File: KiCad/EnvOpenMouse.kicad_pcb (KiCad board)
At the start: 2 copper layers, 34 x 106.6 mm, 117 parts, among them J1 Button, J10 0.8mm BM03B, J11 Conn_02x02_Top_Bottom, J12 0.8mm BM03B, J13 0.8mm BM03B, J2 Conn_01x03, J3 Button, J4 Conn_02x02_Top_Bottom, J5 Conn_02x02_Top_Bottom, J6 Conn_02x02_Top_Bottom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

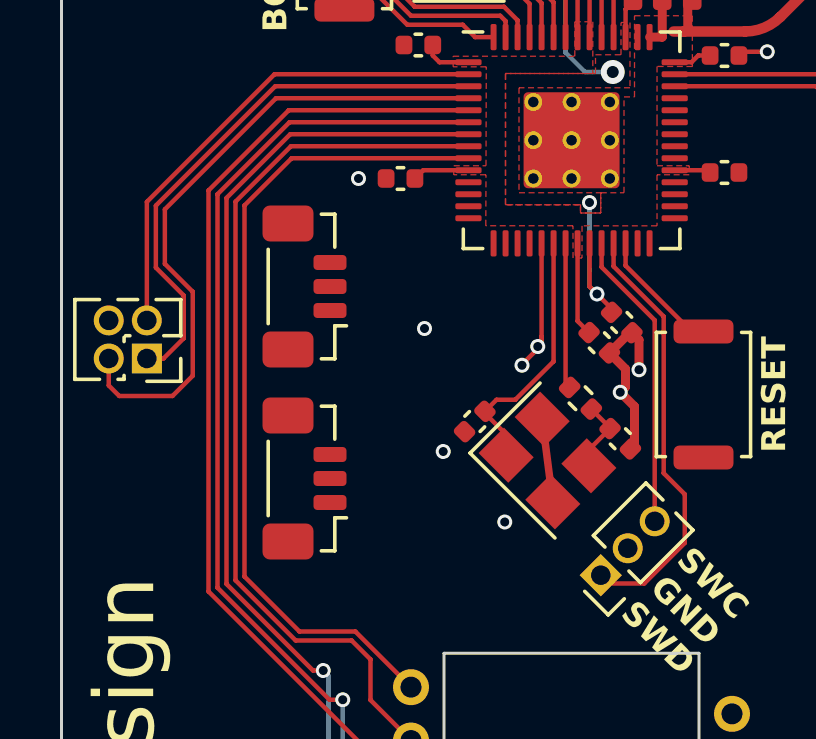
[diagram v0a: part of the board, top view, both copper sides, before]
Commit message: Added missing connections.
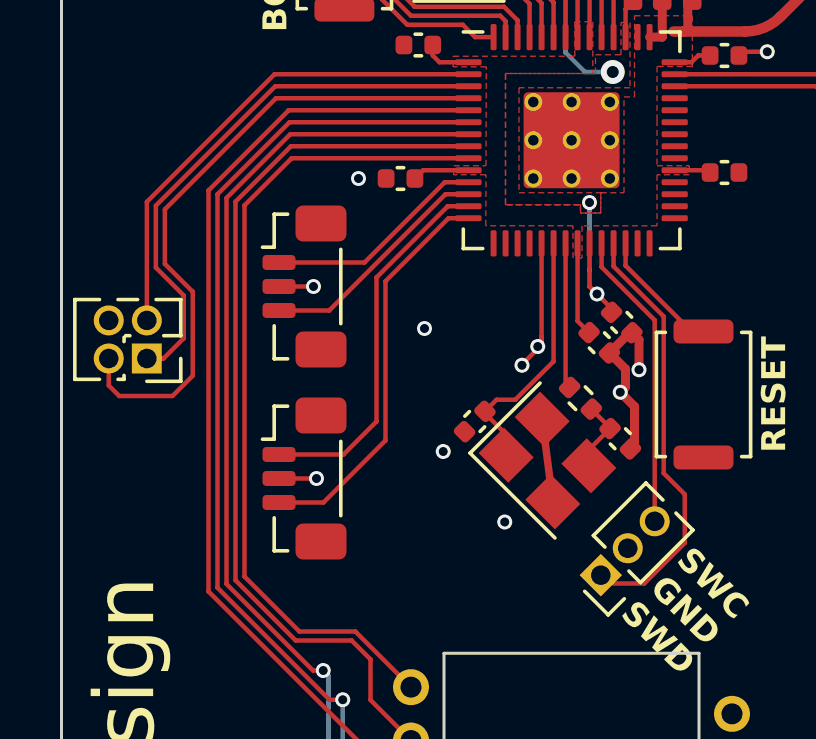
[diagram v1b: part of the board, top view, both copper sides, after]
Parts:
- turned J12 to -90 degrees
- turned J13 to -90 degrees
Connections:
- U3 pad 11: /RP2040/GPIO8 -> SB-1-A_MB
- U3 pad 12: /RP2040/GPIO9 -> SB-2-A_MB
- U3 pad 13: /RP2040/GPIO10 -> SB-3-A_MB
- U3 pad 14: /RP2040/GPIO11 -> SB-4-A_MB
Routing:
- net SB-4-A_MB: track 0.00 -> 13.3 mm
- net SB-3-A_MB: track 0.00 -> 12.6 mm
- net SB-2-A_MB: track 0.00 -> 7.92 mm
- net SB-1-A_MB: track 0.00 -> 7.42 mm
- net GND: track 73.0 -> 75.4 mm, vias 12 -> 14

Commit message: double checked board and tidied things up.
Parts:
- R10, R9: value 27Ohms 0402 Resistor -> 27Ohms 0402 Resistor

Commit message: downsized main board, added more buttons and respective connector, improved spacing of various power traces
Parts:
- removed REF** (x3), REF**1 (x3), REF**10 (x2), REF**11 (x2), REF**12 (x2), REF**13 (x2), REF**14 (x2), REF**15 (x3), REF**16 (x3), REF**17 (x3), REF**18 (x3), REF**19 (x3), REF**2 (x3), REF**3 (x3), REF**4 (x3), REF**5 (x2), REF**6 (x2), REF**7 (x2), REF**8 (x2), REF**9 (x2): NPTH, PCM_kikit:NPTH
- added H5: MountingHole_Pad, MountingHole:MountingHole_2.2mm_M2, F.Cu at (48.4, 126.5)
- added H6: MountingHole_Pad, MountingHole:MountingHole_2.2mm_M2, F.Cu at (76.7, 126.5)
- added J14: 0.8mm BM03B, Connector_JST:JST_SUR_BM03B-SURS-TF_1x03-1MP_P0.80mm_Vertical, F.Cu at (62.5, 126.5)
- added J15: 0.8mm BM03B, Connector_JST:JST_SUR_BM03B-SURS-TF_1x03-1MP_P0.80mm_Vertical, F.Cu at (47.8, 67.1)
- added SW8: SW_Push_SPDT, Button_Switch_SMD:SW_SPST_B3U-1000P, F.Cu at (56.5, 126.5)
- added SW9: SW_Push_SPDT, Button_Switch_SMD:SW_SPST_B3U-1000P, F.Cu at (68.5, 126.5)
- moved J13 9.40 mm to (47.8, 60.6)
- moved J12 9.32 mm to (47.8, 54.1)
- moved H1 5.05 mm to (48.0, 76.0)
- moved H4 5.05 mm to (76.9, 76.0)
- moved H5 5.05 mm to (48.4, 114.5)
- moved H6 5.05 mm to (76.7, 114.5)
- moved H7 5.05 mm to (76.6, 120.5)
- moved H8 5.05 mm to (48.4, 120.5)
- moved J10 5.05 mm to (62.5, 120.5)
- moved J4 5.05 mm to (56.1, 82.9)
- moved J5 5.05 mm to (48.4, 108.4)
- moved J6 5.05 mm to (77.9, 108.5)
- moved J9 5.05 mm to (62.5, 114.5)
- moved SW1 5.05 mm to (72.0, 102.2)
- moved SW2 5.05 mm to (51.6, 86.9)
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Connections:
- U3 pad 15: /RP2040/GPIO12 -> SB-5-A_MB
- U3 pad 16: /RP2040/GPIO13 -> SB-6-A_MB
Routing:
- net GND: track 75.4 -> 108.5 mm, vias 14 -> 12
- net SB-6-A_MB: track 0.00 -> 31.3 mm, vias 0 -> 2
- net SB-5-A_MB: track 0.00 -> 30.2 mm, vias 0 -> 2
- net SB-2-A_MB: track 7.92 -> 19.0 mm, vias 0 -> 2
- net SB-3-A_MB: track 12.6 -> 23.5 mm, vias 0 -> 2
- net SB-1-A_MB: track 7.42 -> 17.9 mm, vias 0 -> 2
- net SB-4-A_MB: track 13.3 -> 23.7 mm, vias 0 -> 2
- net VBUS: track 11.5 -> 19.9 mm
- net SB-5-A: track 0.00 -> 4.40 mm
- net SB-6-A: track 0.00 -> 4.40 mm
- net USB_D-: track 10.3 -> 13.3 mm
- net /RP2040/SWCLK: track 10.00 -> 10.8 mm
- net +1V8: track 69.0 -> 68.3 mm
- net /RP2040/SWD: track 14.4 -> 15.0 mm
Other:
- board size 34 x 106.6 mm -> 34 x 107.5 mm

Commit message: added header for unused GPIOs
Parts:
- added J16: Conn_01x14, Connector_PinHeader_1.00mm:PinHeader_1x14_P1.00mm_Vertical, F.Cu at (71.3, 54.4)
- moved C17 0.81 mm to (68.2, 43.6), turned to -45 degrees
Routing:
- net /RP2040/GPIO14: track 0.00 -> 19.3 mm, vias 0 -> 1
- net /RP2040/GPIO15: track 0.00 -> 18.1 mm, vias 0 -> 1
- net /RP2040/GPIO16: track 0.00 -> 11.0 mm
- net /RP2040/GPIO17: track 0.00 -> 9.85 mm
- net /RP2040/GPIO18: track 0.00 -> 8.72 mm
- net /RP2040/GPIO19: track 0.00 -> 8.26 mm
- net /RP2040/GPIO20: track 0.00 -> 7.37 mm
- net /RP2040/GPIO22: track 0.00 -> 7.28 mm
- net /RP2040/GPIO21: track 0.00 -> 7.03 mm
- net /RP2040/GPIO23: track 0.00 -> 6.70 mm
- net /RP2040/GPIO24: track 0.00 -> 6.45 mm
- net /RP2040/GPIO25: track 0.00 -> 6.20 mm
- net /RP2040/GPIO26_ADC0: track 0.00 -> 5.95 mm
- net /RP2040/GPIO27_ADC1: track 0.00 -> 5.70 mm
- net MB-1-A_MB: track 17.3 -> 22.0 mm
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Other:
- board text added: "GP27 GP26 GP25 GP24 GP23 GP22 GP21 GP20 GP19 GP18 GP17 GP16 GP15 GP14"

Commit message: generated production files
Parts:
- J4: footprint Connector_PinHeader_1.27mm:PinHeader_1x02_P1.27mm_Vertical -> Connector_PinSocket_1.27mm:PinSocket_1x02_P1.27mm_Vertical; moved to B.Cu
- turned J4 to 0 degrees

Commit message: final cleanups and other fixes
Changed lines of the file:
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@@
 		(tags "Through hole socket strip THT 1x02 1.27mm single row")
 		(property "Reference" "J4"
-			(at 0 2.135 360)
+			(at 0 2.135 0)
 			(layer "B.SilkS")
 			(hide yes)
@@
 		)
 		(property "Value" "Conn_02x02_Top_Bottom"
-			(at 0 -3.405 360)
+			(at 0 -3.405 0)
 			(layer "B.Fab")
 			(effects
@@
 	)
 	(gr_text "SWC\nGND\nSWD"
-		(at 63.95 55.65 0)
+		(at 64.35 55.65 0)
 		(layer "F.SilkS")
 		(effects

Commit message: updated part values, generated production files
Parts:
- D1: value 1n4002W -> 1n5819W
- J1, J3: value Button -> B3U-1000P
- J11, J7, J8: value Conn_02x02_Top_Bottom -> Conn_02x02 Pins
- J4, J5, J6: value Conn_02x02_Top_Bottom -> Conn_02x02 Socket
- SW1, SW2, SW3: value SW_Push_SPDT -> Kailh GM switch
- SW4, SW5, SW6, SW7, SW8, SW9: value SW_Push_SPDT -> B3U-1000P
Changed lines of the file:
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@@
 			)
 		)
-		(property "Value" "SW_Push_SPDT"
+		(property "Value" "B3U-1000P"
 			(at 0 2.5 180)
 			(layer "F.Fab")
@@
 		(sheetname "Root")
 		(sheetfile "EnvOpenMouse.kicad_sch")
-		(attr exclude_from_pos_files)
+		(attr exclude_from_pos_files exclude_from_bom)
 		(fp_circle
 			(center 0 0)
@@
 		(sheetname "Root")
 		(sheetfile "EnvOpenMouse.kicad_sch")
-		(attr exclude_from_pos_files)
+		(attr exclude_from_pos_files exclude_from_bom)
 		(fp_circle
 			(center 0 0)
@@
 		(sheetname "Root")
 		(sheetfile "EnvOpenMouse.kicad_sch")
-		(attr exclude_from_pos_files)
+		(attr exclude_from_pos_files exclude_from_bom)
 		(fp_circle
 			(center 0 0)
@@
 		(sheetname "Root")
 		(sheetfile "EnvOpenMouse.kicad_sch")
-		(attr exclude_from_pos_files)
+		(attr exclude_from_pos_files exclude_from_bom)
 		(fp_circle
 			(center 0 0)
@@
 			)
 		)
-		(property "Value" "1n4002W"
+		(property "Value" "1n5819W"
 			(at 0 2.1 0)
 			(layer "F.Fab")
@@
 			)
 		)
-		(property "Value" "SW_Push_SPDT"
+		(property "Value" "Kailh GM switch"
 			(at 0 -7.62 0)
 			(layer "F.Fab")
@@
 		(sheetname "Root")
 		(sheetfile "EnvOpenMouse.kicad_sch")
-		(attr exclude_from_pos_files)
+		(attr exclude_from_pos_files exclude_from_bom)
 		(fp_circle
 			(center 0 0)
@@
 			)
 		)
-		(property "Value" "SW_Push_SPDT"
+		(property "Value" "B3U-1000P"
 			(at 0 2.5 0)
 			(layer "F.Fab")
@@
 			)
 		)
-		(property "Value" "SW_Push_SPDT"
+		(property "Value" "Kailh GM switch"
 			(at 0 -7.62 0)
 			(layer "F.Fab")
@@
 		(sheetname "Root")
 		(sheetfile "EnvOpenMouse.kicad_sch")
-		(attr exclude_from_pos_files)
+		(attr exclude_from_pos_files exclude_from_bom)
 		(fp_circle
 			(center 0 0)
@@
 			)
 		)
-		(property "Value" "Conn_02x02_Top_Bottom"
+		(property "Value" "Conn_02x02 Pins"
 			(at 0.635 2.965 0)
 			(layer "F.Fab")
@@
 		(sheetname "Root")
 		(sheetfile "EnvOpenMouse.kicad_sch")
-		(attr exclude_from_pos_files)
+		(attr exclude_from_pos_files exclude_from_bom)
 		(fp_circle
 			(center 0 0)
@@
 			)
 		)
-		(property "Value" "Button"
+		(property "Value" "B3U-1000P"
 			(at 0 2.5 90)
 			(layer "F.Fab")
@@
 		(sheetname "Root")
 		(sheetfile "EnvOpenMouse.kicad_sch")
-		(attr exclude_from_pos_files)
+		(attr exclude_from_pos_files exclude_from_bom)
 		(fp_circle
 			(center 0 0)
@@
 		(sheetname "Root")
 		(sheetfile "EnvOpenMouse.kicad_sch")
-		(attr exclude_from_pos_files)
+		(attr exclude_from_pos_files exclude_from_bom)
 		(fp_circle
 			(center 0 0)
@@
 			)
 		)
-		(property "Value" "SW_Push_SPDT"
+		(property "Value" "B3U-1000P"
 			(at 0 2.5 0)
 			(layer "F.Fab")
@@
 		(sheetname "Root")
 		(sheetfile "EnvOpenMouse.kicad_sch")
-		(attr exclude_from_pos_files)
+		(attr exclude_from_pos_files exclude_from_bom)
 		(fp_circle
 			(center 0 0)
@@
 			)
 		)
-		(property "Value" "SW_Push_SPDT"
+		(property "Value" "B3U-1000P"
 			(at 0 2.5 0)
 			(layer "F.Fab")
@@
 			)
 		)
-		(property "Value" "Button"
+		(property "Value" "B3U-1000P"
 			(at 0 2.5 90)
 			(layer "F.Fab")
@@
 			)
 		)
-		(property "Value" "Conn_02x02_Top_Bottom"
+		(property "Value" "Conn_02x02 Socket"
 			(at 0.635 2.965 0)
 			(layer "F.Fab")
@@
 			)
 		)
-		(property "Value" "SW_Push_SPDT"
+		(property "Value" "B3U-1000P"
 			(at 0 2.5 180)
 			(layer "F.Fab")
@@
 			)
 		)
-		(property "Value" "SW_Push_SPDT"
+		(property "Value" "B3U-1000P"
 			(at 0 2.5 0)
 			(layer "F.Fab")
@@
 			)
 		)
-		(property "Value" "Conn_02x02_Top_Bottom"
+		(property "Value" "Conn_02x02 Socket"
 			(at 0.635 2.965 0)
 			(layer "F.Fab")
@@
 			)
 		)
-		(property "Value" "SW_Push_SPDT"
+		(property "Value" "Kailh GM switch"
 			(at 0 -7.62 0)
 			(layer "F.Fab")
@@
 			)
 		)
-		(property "Value" "Conn_02x02_Top_Bottom"
+		(property "Value" "Conn_02x02 Pins"
 			(at 0.635 2.965 0)
 			(layer "F.Fab")
@@
 			)
 		)
-		(property "Value" "Conn_02x02_Top_Bottom"
+		(property "Value" "Conn_02x02 Pins"
 			(at 0 2.965 0)
 			(layer "F.Fab")
@@
 			)
 		)
-		(property "Value" "Conn_02x02_Top_Bottom"
+		(property "Value" "Conn_02x02 Socket"
 			(at 0 -3.405 0)
 			(layer "B.Fab")

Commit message: generated fixes production files
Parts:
- J5, J6: footprint Connector_PinHeader_1.27mm:PinHeader_2x02_P1.27mm_Vertical -> Connector_PinSocket_1.27mm:PinSocket_2x02_P1.27mm_Vertical; moved to B.Cu
- turned J5 to 0 degrees
- turned J6 to 0 degrees
